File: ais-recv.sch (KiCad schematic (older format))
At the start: 46 parts, among them J1 Conn_02x05_Odd_Even, J2 CONSMA 003.062, J3 105017-0001, SW1 SW_Push, U1 NCP115ASN330T1G, U2 Si4362-C, U3 STM32L072KZUx, U4 USBLC6-2SC6, U5 Si4362-C, Y1 30 MHz, Y2 32.768 kHz

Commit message: Use STML4
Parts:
- removed C23: 0.1 uF, IPC7351-Least:CAPC1005X55, symbol Device:C
- removed U3: STM32L072KZUx, local:QFN50P500X500X80-33-THERMALVIAS, symbol MCU_ST_STM32L0:STM32L072KZUx
- removed Y2: 32.768 kHz, local:Crystal_SMD_2012-2Pin_2.0x1.2mm, symbol Device:Crystal
- added U3: STM32L432KCUx, local:QFN50P500X500X80-33-THERMALVIAS, symbol MCU_ST_STM32L4:STM32L432KCUx
- renumbered C24 to C23
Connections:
- net BOOT0: now also U3.31 (PH3)
- net CH1_CTS: now also U3.7 (PA1)
- net CH1_SDN: now also U3.9 (PA3)
- net CH2_CTS: now also U3.18 (PA8)
- net CH2_SDN: now also U3.19 (PA9)
- net GND: now also U3.16 (VSS), U3.32 (VSS), U3.33 (VSS)
- net SPI_CLK: now also U3.11 (PA5)
- net SPI_MISO: now also U3.12 (PA6)
- net SPI_MOSI: now also U3.13 (PA7)
- net SWDCLK: now also U3.24 (PA14)
- net SWDIO: now also U3.23 (PA13)
- net UART1_RX: now also U3.30 (PB7)
- net UART1_TX: now also U3.29 (PB6)
- net USB_D+: now also U3.22 (PA12)
- net USB_D-: now also U3.21 (PA11)
- net VDD: now also U3.1 (VDD), U3.17 (VDD), U3.5 (VDDA)
- net ~CH1_IRQ: now also U3.6 (PA0)
- net ~CH1_SEL: now also U3.10 (PA4)
- net ~CH2_IRQ: now also U3.8 (PA2)
- net ~CH2_SEL: now also U3.20 (PA10)
- net ~RESET: now also U3.4 (NRST)
- no-connect marks 12 -> 16
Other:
- note added: "WKUP1"
- note added: "WKUP4"
- note removed: "Use STM32L432KCUx instead"
- moved on the sheet: C23, R2, SW1

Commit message: Changes for version 1.0
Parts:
- removed SW1: SW_Push, local:SW_SPST_PTS_540, symbol Switch:SW_Push
- added C14: DNP, IPC7351-Least:CAPC1005X55, symbol Device:C_Small
- added FB2, FB3, FB4: 220 Ohm, IPC7351-Least:INDC1005X60, symbol Device:Ferrite_Bead
- added J1: FTS-105-01-L-S, Connector_PinHeader_1.27mm:PinHeader_1x05_P1.27mm_Vertical, symbol Connector_Generic:Conn_01x05
- FB1: value Ferrite_Bead -> 220 Ohm; MFG Name (none) -> TDK; MFG Part Num (none) -> MPZ1005S221HT000
- J2: renamed from J1; value Conn_02x05_Odd_Even -> TMS-105-01-L-D; MFG Name (none) -> Samtec; MFG Part Num (none) -> TMS-105-01-L-D
- L3: value L -> 270 nH
- L6: footprint IPC7351-Least:INDC1608X95 -> IPC7351-Least:INDC1005X60
- U1: symbol Regulator_Linear:TC1017-xCT -> local:TC1017-xCT
- renumbered C4 to C1, C13 to C10, C14 to C11, C15 to C12, C16 to C13, C1 to C15, C2 to C16, C3 to C17, C17 to C18, C18 to C19, C5 to C2, C19 to C20, C20 to C21, C21 to C23, C23 to C24, C6 to C3, C7 to C4, C8 to C5, C9 to C6, C10 to C7, C11 to C8, C12 to C9, J2 to J3, J3 to J4
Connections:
- net BOOT0: now also J1.2 (Pin_2); no longer J2.5 (Pin_5)
- net GND: now also J2.5 (Pin_5), J2.7 (Pin_7), C14.2, J1.5 (Pin_5)
- net UART1_RX: now also J1.3 (Pin_3); no longer J2.8 (Pin_8)
- net UART1_TX: now also J1.4 (Pin_4); no longer J2.6 (Pin_6)
- net VDD: now also FB2.2, FB3.2, FB4.2, J1.1 (Pin_1); no longer C15.1, C16.1, C17.1, C18.1, C19.1, C20.1, C23.1, C24.1, U2.6 (VDD), U2.8 (VDD), U3.5 (VDDA), U5.6 (VDD), U5.8 (VDD)
- net ~CH1_IRQ: now also U3.14 (PB0); no longer U3.6 (PA0)
- net ~CH1_SEL: now also U3.9 (PA3); no longer U3.10 (PA4)
- net ~CH2_IRQ: now also U3.28 (PB5); no longer U3.8 (PA2)
- net CH1_RX_CLK: now reaches U2.19 (GPIO2)
- net CH1_RX_CLK: now also U3.8 (PA2)
- net CH1_RX_DATA: now reaches U2.20 (GPIO3)
- net CH1_RX_DATA: now also U3.6 (PA0)
- net CH2_RX_CLK: now reaches U5.19 (GPIO2)
- net CH2_RX_CLK: now also U3.10 (PA4)
- net CH2_RX_DATA: now reaches U5.20 (GPIO3)
- net CH2_RX_DATA: now also U3.19 (PA9)
- net at J4.6 (Shield), L6.1: now also C14.1
- net SDN: now reaches U3.25 (PA15)
- net SDN: now also U2.1 (SDN), U5.1 (SDN)
- net SWO: now reaches U3.26 (PB3)
- net SWO: now also J2.6 (Pin_6)
- removed net CH1_SDN: U2.1 (SDN), U3.9 (PA3)
- removed net CH2_SDN: U3.19 (PA9), U5.1 (SDN)
- new net VDDA: C23.1, C24.1, FB4.1, U3.5 (VDDA)
- new net VDD_RF1: C15.1, C16.1, C17.1, FB2.1, U2.6 (VDD), U2.8 (VDD)
- new net VDD_RF2: C18.1, C19.1, C20.1, FB3.1, U5.6 (VDD), U5.8 (VDD)
- no-connect marks 16 -> 8
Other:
- note removed: "WKUP1"
- note removed: "WKUP4"
- moved on the sheet: C15, C16, C17, C18, C19, C20, C21, C22, C23, C24, J2

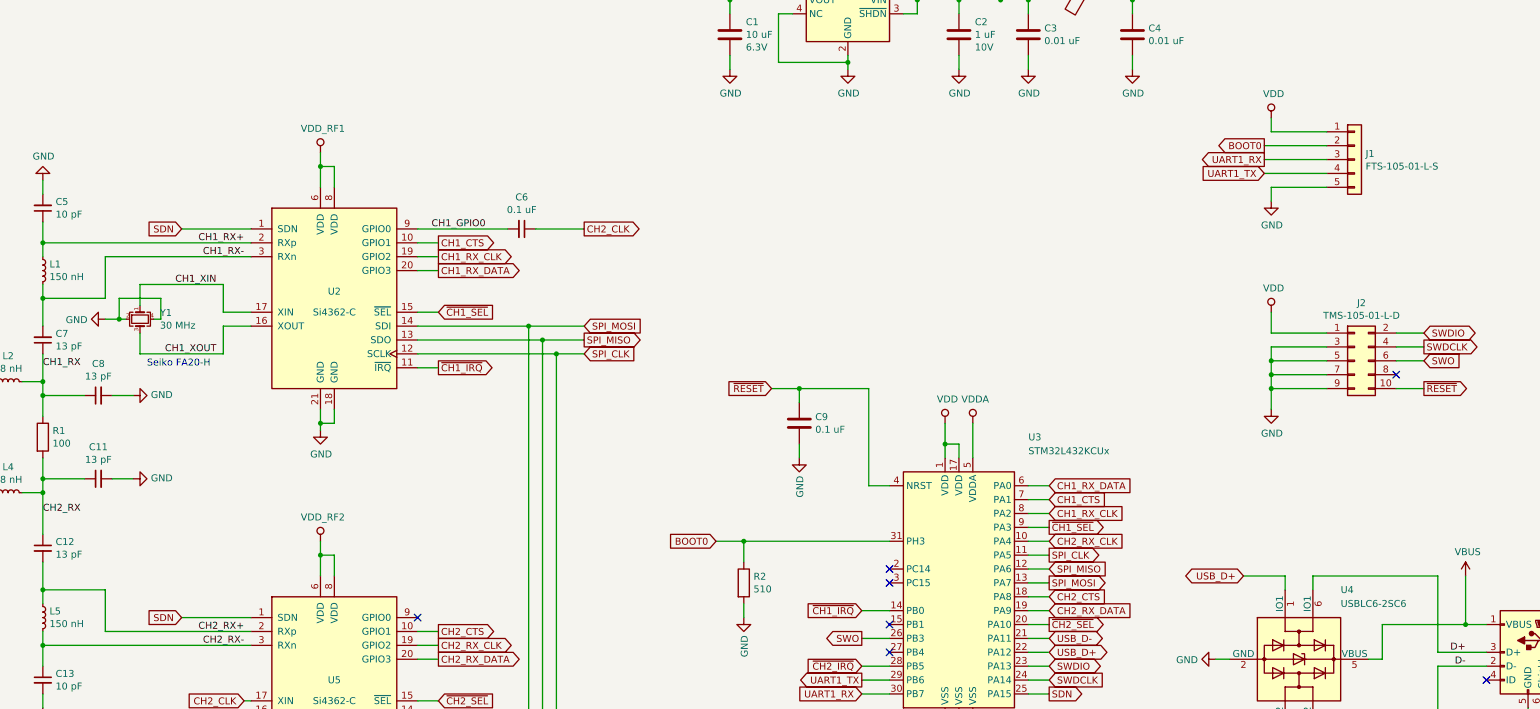
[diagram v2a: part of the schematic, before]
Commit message: Fix part numbers for the debug connector, USB ESD diodes, quartz
Add a note about wrong quartz frequency.
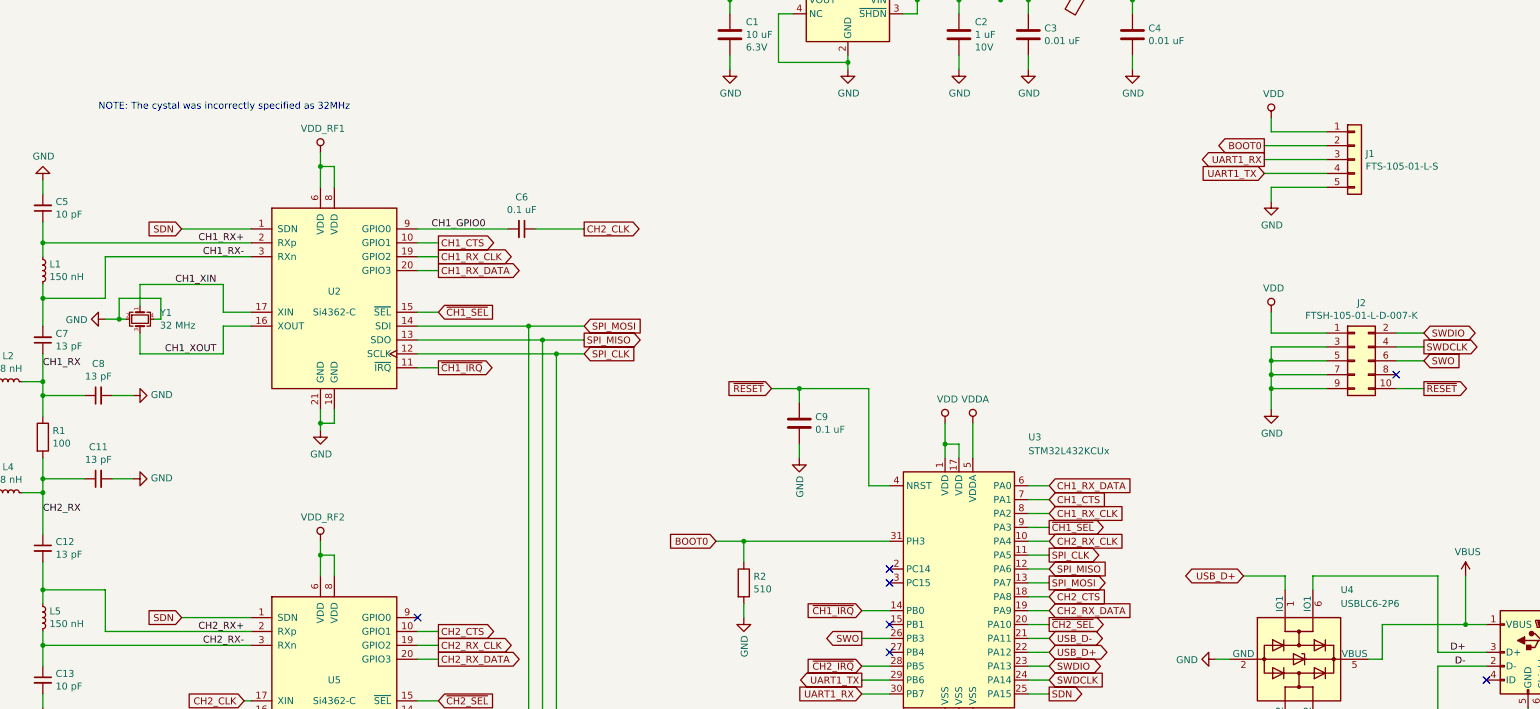
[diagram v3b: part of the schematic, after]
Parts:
- J2: value TMS-105-01-L-D -> FTSH-105-01-L-D-007-K; MFG Part Num TMS-105-01-L-D -> FTSH-105-01-L-D-007-K
- U4: value USBLC6-2SC6 -> USBLC6-2P6; MFG Name (none) -> ST; MFG Part Num (none) -> USBLC6-2P6
- Y1: value 30 MHz -> 32 MHz
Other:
- note added: "NOTE: The cystal was incorrectly specified as 32MHz"
- note removed: "Seiko FA20-H"
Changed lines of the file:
@@
 P 5000 3900
 F 0 "Y1" V 4954 4044 50  0000 L CNN
-F 1 "30 MHz" V 5045 4044 50  0000 L CNN
+F 1 "32 MHz" V 5045 4044 50  0000 L CNN
 F 2 "IPC7351-Least:OSCCC200X250X080" H 5000 3900 50  0001 C CNN
 F 3 "~" H 5000 3900 50  0001 C CNN
@@
 	1    0    0    -1
 $EndComp
-Text Notes 5050 4250 0    50   ~ 0
-Seiko FA20-H
 Text GLabel 11550 6100 2    50   Output ~ 0
 ~CH2_SEL
@@
 P 13750 4200
 F 0 "J2" H 13800 4617 50  0000 C CNN
-F 1 "TMS-105-01-L-D" H 13800 4526 50  0000 C CNN
+F 1 "FTSH-105-01-L-D-007-K" H 13800 4526 50  0000 C CNN
 F 2 "local:PinHeader_2x05_P1.27mm_Vertical" H 13750 4200 50  0001 C CNN
 F 3 "~" H 13750 4200 50  0001 C CNN
 F 4 "Samtec" H 13750 4200 50  0001 C CNN "MFG Name"
-F 5 "TMS-105-01-L-D" H 13750 4200 50  0001 C CNN "MFG Part Num"
+F 5 "FTSH-105-01-L-D-007-K" H 13750 4200 50  0001 C CNN "MFG Part Num"
 	1    13750 4200
 	1    0    0    -1
@@
 P 13350 6350
 F 0 "U4" V 12850 6650 50  0000 L CNN
-F 1 "USBLC6-2SC6" V 12950 6650 50  0000 L CNN
+F 1 "USBLC6-2P6" V 12950 6650 50  0000 L CNN
 F 2 "local:SOT-666" H 12600 6750 50  0001 C CNN
 F 3 "http://www2.st.com/resource/en/datasheet/CD00050750.pdf" H 13550 6700 50  0001 C CNN
+F 4 "ST" H 13350 6350 50  0001 C CNN "MFG Name"
+F 5 "USBLC6-2P6" H 13350 6350 50  0001 C CNN "MFG Part Num"
 	1    13350 6350
 	0    1    1    0
@@
 Wire Wire Line
 	9600 1700 9700 1700
+Text Notes 4700 2400 0    50   ~ 0
+NOTE: The cystal was incorrectly specified as 32MHz
 $EndSCHEMATC

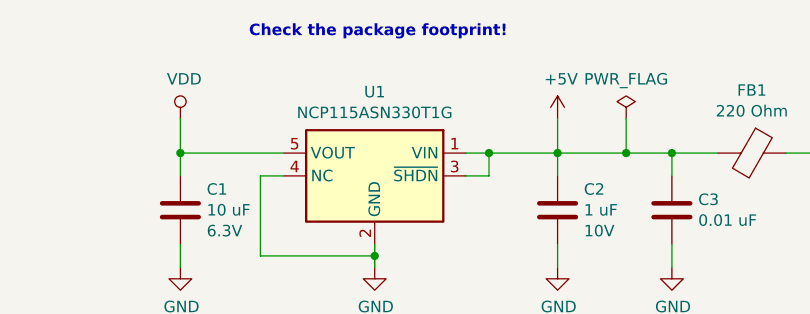
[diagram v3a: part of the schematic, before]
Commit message: Remove a note about checking a footprint
The footprint is correct.
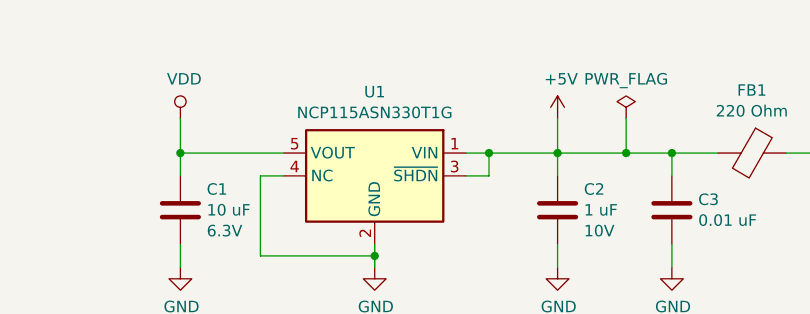
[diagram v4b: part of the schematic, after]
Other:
- note removed: "Check the package footprint!"
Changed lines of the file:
@@
 	-1   0    0    -1
 $EndComp
-Text Notes 9550 1100 0    50   ~ 10
-Check the package footprint!
 Wire Wire Line
 	10500 1700 10600 1700
